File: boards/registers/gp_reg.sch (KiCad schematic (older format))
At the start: 22 parts

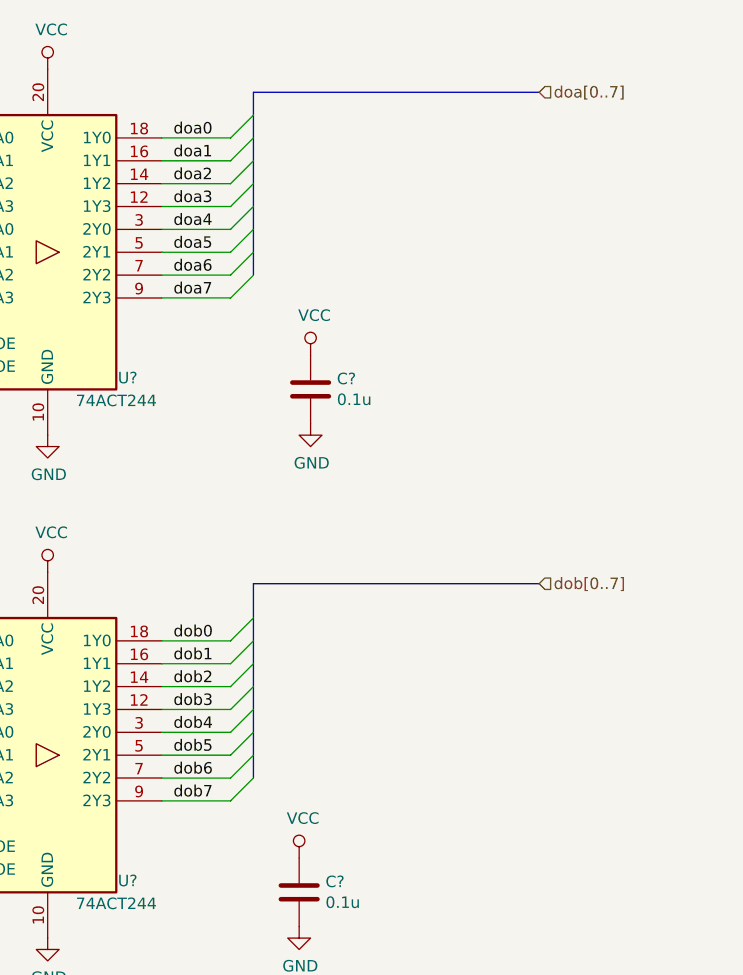
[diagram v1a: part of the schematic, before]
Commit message: Add bus resistors
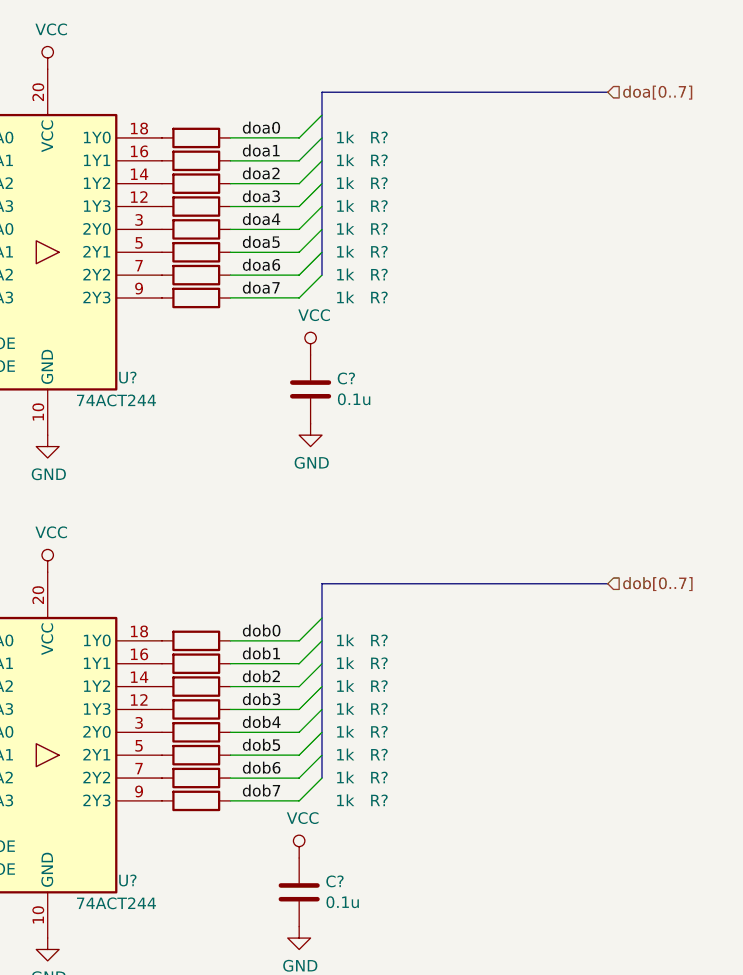
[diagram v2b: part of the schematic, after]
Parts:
- added R? (x16): 1k, symbol Device:R
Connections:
- net doa0: now also R?.1; no longer U?.18 (1Y0)
- net doa1: now also R?.1; no longer U?.16 (1Y1)
- net doa2: now also R?.1; no longer U?.14 (1Y2)
- net doa3: now also R?.1; no longer U?.12 (1Y3)
- net doa4: now also R?.1; no longer U?.3 (2Y0)
- net doa5: now also R?.1; no longer U?.5 (2Y1)
- net doa6: now also R?.1; no longer U?.7 (2Y2)
- net doa7: now also R?.1; no longer U?.9 (2Y3)
- net dob0: now also R?.1; no longer U?.18 (1Y0)
- net dob1: now also R?.1; no longer U?.16 (1Y1)
- net dob2: now also R?.1; no longer U?.14 (1Y2)
- net dob3: now also R?.1; no longer U?.12 (1Y3)
- net dob4: now also R?.1; no longer U?.3 (2Y0)
- net dob5: now also R?.1; no longer U?.5 (2Y1)
- net dob6: now also R?.1; no longer U?.7 (2Y2)
- net dob7: now also R?.1; no longer U?.9 (2Y3)
- new net: R?.2, U?.12 (1Y3) (x2)
- new net: R?.2, U?.14 (1Y2) (x2)
- new net: R?.2, U?.16 (1Y1) (x2)
- new net: R?.2, U?.18 (1Y0) (x2)
- new net: R?.2, U?.3 (2Y0) (x2)
- new net: R?.2, U?.5 (2Y1) (x2)
- new net: R?.2, U?.7 (2Y2) (x2)
- new net: R?.2, U?.9 (2Y3) (x2)

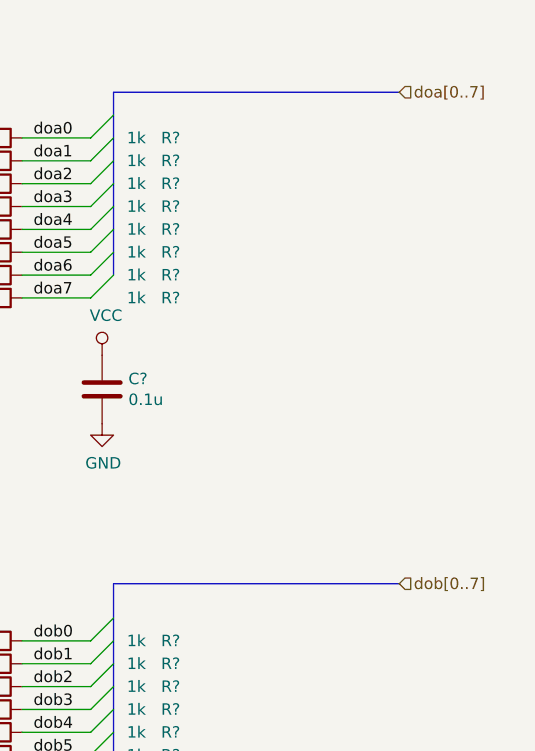
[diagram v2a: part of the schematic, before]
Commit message: Remove redundant chip from the register A, change hierarchical pin types
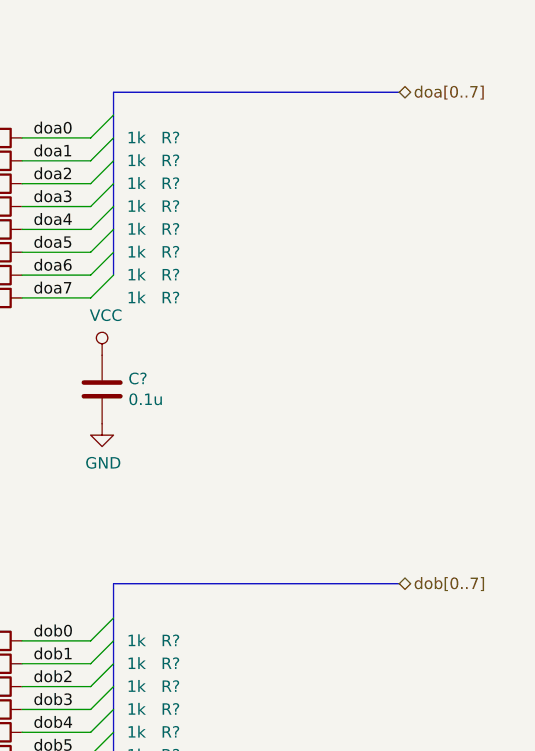
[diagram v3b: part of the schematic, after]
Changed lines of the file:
@@
 $Descr A4 11693 8268
 encoding utf-8
-Sheet 6 6
+Sheet 5 7
 Title "General-purpose register"
 Date "2019-12-29"
@@
 Text HLabel 1200 950  0    50   Input ~ 0
 di[0..7]
-Text HLabel 9250 950  2    50   Input ~ 0
+Text HLabel 9250 950  2    50   3State ~ 0
 doa[0..7]
-Text HLabel 9250 3100 2    50   Input ~ 0
+Text HLabel 9250 3100 2    50   3State ~ 0
 dob[0..7]
 $Comp

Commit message: Fix unconnected nets
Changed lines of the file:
@@
 AR Path="/5E73B7F6/5E73BC4E" Ref="U?"  Part="1"
 AR Path="/5E7CA397/5E73BC4E" Ref="U?"  Part="1"
-F 0 "U?" H 7150 1100 50  0000 C CNN
+F 0 "U?" H 7200 1100 50  0000 C CNN
 F 1 "74ACT244" H 7100 1000 50  0000 C CNN
 F 2 "" H 6800 1650 50  0001 C CNN
@@
 AR Path="/5E73B7F6/5E74CA38" Ref="U?"  Part="1"
 AR Path="/5E7CA397/5E74CA38" Ref="U?"  Part="1"
-F 0 "U?" H 7150 3300 50  0000 C CNN
+F 0 "U?" H 7200 3300 50  0000 C CNN
 F 1 "74ACT244" H 7100 3200 50  0000 C CNN
 F 2 "" H 6800 3850 50  0001 C CNN
@@
 AR Path="/5E73B7F6/5E755BB1" Ref="U?"  Part="1"
 AR Path="/5E7CA397/5E755BB1" Ref="U?"  Part="1"
-F 0 "U?" H 4650 1100 50  0000 C CNN
+F 0 "U?" H 4700 1100 50  0000 C CNN
 F 1 "74AC273" H 4650 1000 50  0000 C CNN
 F 2 "" H 4300 1650 50  0001 C CNN

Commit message: Annotated schematics, assigned footprints
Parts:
- C25, C26, C27: renamed from C?; footprint (none) -> Capacitor_SMD:C_0805_2012Metric
- D46, D47, D48, D49, D50, D51, D52, D53: renamed from D?; footprint (none) -> LED_SMD:LED_0805_2012Metric
- R126, R127, R128, R129, R130, R131, R132, R133, R134, R135, R136, R137, R138, R139, R140, R141, R142, R143, R144, R145, R146, R147, R148, R149: renamed from R?; footprint (none) -> Resistor_SMD:R_0805_2012Metric
- U25: renamed from U?; footprint (none) -> Package_SO:SOIC-20W_7.5x12.8mm_P1.27mm
- U26, U27: renamed from U?; footprint (none) -> Package_SO:SO-20_12.8x7.5mm_P1.27mm
